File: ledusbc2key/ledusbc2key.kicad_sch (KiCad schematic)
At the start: 25 parts, among them SW1 SW_Push, U1 ATmega32U2-A, U2 PRTR5V0U2X, Y1 Crystal_GND24_Small

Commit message: did a bit today
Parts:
- removed MX3: MX-NoLED, symbol MX_Alps_Hybrid:MX-NoLED
- C7, C8: footprint Capacitor_SMD:C_0805_2012Metric_Pad1.15x1.40mm_HandSolder -> Capacitor_SMD:C_0805_2012Metric_Pad1.18x1.45mm_HandSolder
- MX1, MX2: footprint (none) -> MX_Alps_Hybrid:MX-1U-NoLED
- R4, R5: footprint Resistor_SMD:R_0805_2012Metric_Pad1.15x1.40mm_HandSolder -> Resistor_SMD:R_0805_2012Metric_Pad1.20x1.40mm_HandSolder
- R6: footprint (none) -> Resistor_SMD:R_0805_2012Metric_Pad1.20x1.40mm_HandSolder
- SW1: footprint (none) -> random-keyboard-parts:SKQGADE010
- Y1: footprint (none) -> Crystal:Crystal_SMD_3225-4Pin_3.2x2.5mm_HandSoldering
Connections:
- net COL2: no longer names the net of U1.18 (PB4)

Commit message: finished 2k
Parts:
- MX1, MX2: footprint MX_Alps_Hybrid:MX-1U-NoLED -> MX_Only:MXOnly-1U-Hotswap
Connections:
- net COL0: now also U1.26 (PC4); no longer U1.16 (PB2)
- net COL1: now also U1.25 (PC5); no longer U1.17 (PB3)
- net LED: now also U1.17 (PB3); no longer U1.23 (PC6)
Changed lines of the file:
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@@
     )
   )
-  (global_label "LED" (shape input) (at 97.79 69.85 0) (fields_autoplaced)
+  (global_label "LED" (shape input) (at 97.79 46.99 0) (fields_autoplaced)
     (effects (font (size 1.27 1.27)) (justify left))
-    (property "Intersheet References" "${INTERSHEET_REFS}" (id 0) (at 103.6502 69.7706 0)
+    (property "Intersheet References" "${INTERSHEET_REFS}" (id 0) (at 103.6502 46.9106 0)
       (effects (font (size 1.27 1.27)) (justify left) hide)
     )
@@
     )
   )
-  (global_label "COL0" (shape input) (at 97.79 44.45 0) (fields_autoplaced)
+  (global_label "COL0" (shape input) (at 97.79 64.77 0) (fields_autoplaced)
     (effects (font (size 1.27 1.27)) (justify left))
-    (property "Intersheet References" "${INTERSHEET_REFS}" (id 0) (at 105.0412 44.3706 0)
+    (property "Intersheet References" "${INTERSHEET_REFS}" (id 0) (at 105.0412 64.6906 0)
       (effects (font (size 1.27 1.27)) (justify left) hide)
     )
@@
     )
   )
-  (global_label "COL1" (shape input) (at 97.79 46.99 0) (fields_autoplaced)
+  (global_label "COL1" (shape input) (at 97.79 67.31 0) (fields_autoplaced)
     (effects (font (size 1.27 1.27)) (justify left))
-    (property "Intersheet References" "${INTERSHEET_REFS}" (id 0) (at 105.0412 46.9106 0)
+    (property "Intersheet References" "${INTERSHEET_REFS}" (id 0) (at 105.0412 67.2306 0)
       (effects (font (size 1.27 1.27)) (justify left) hide)
     )
@@
       (effects (font (size 0.508 0.508)))
     )
-    (property "Footprint" "MX_Alps_Hybrid:MX-1U-NoLED" (id 2) (at 114.935 40.005 0)
+    (property "Footprint" "MX_Only:MXOnly-1U-Hotswap" (id 2) (at 114.935 40.005 0)
       (effects (font (size 1.524 1.524)) hide)
     )
@@
       (effects (font (size 0.508 0.508)))
     )
-    (property "Footprint" "MX_Alps_Hybrid:MX-1U-NoLED" (id 2) (at 98.425 40.005 0)
+    (property "Footprint" "MX_Only:MXOnly-1U-Hotswap" (id 2) (at 98.425 40.005 0)
       (effects (font (size 1.524 1.524)) hide)
     )
@@
     )
     (path "/f9445bf9-6026-4cdf-b33a-84c971e8abe4"
-      (reference "MX1") (unit 1) (value "MX-NoLED") (footprint "MX_Alps_Hybrid:MX-1U-NoLED")
+      (reference "MX1") (unit 1) (value "MX-NoLED") (footprint "MX_Only:MXOnly-1U-Hotswap")
     )
     (path "/9652c5be-ceda-40bb-9f68-e3e71dd4d91a"
-      (reference "MX2") (unit 1) (value "MX-NoLED") (footprint "MX_Alps_Hybrid:MX-1U-NoLED")
+      (reference "MX2") (unit 1) (value "MX-NoLED") (footprint "MX_Only:MXOnly-1U-Hotswap")
     )
     (path "/7ad95de5-26a3-4aff-83fa-e71036fd37d6"

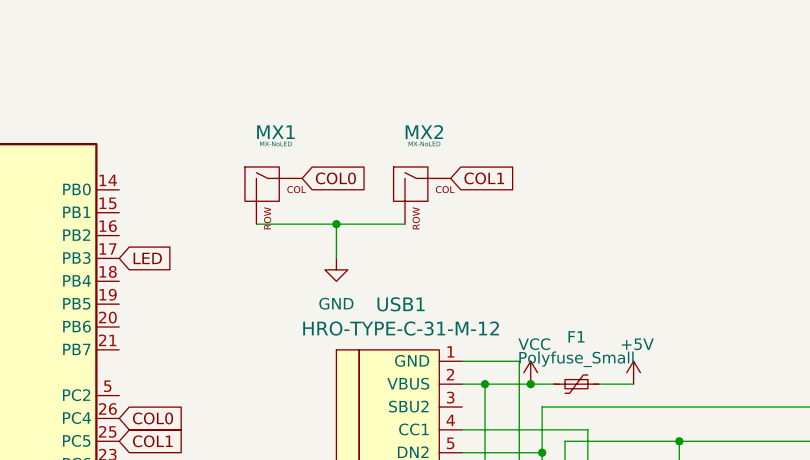
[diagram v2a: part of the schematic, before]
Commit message: swapped to new library for ledusbc
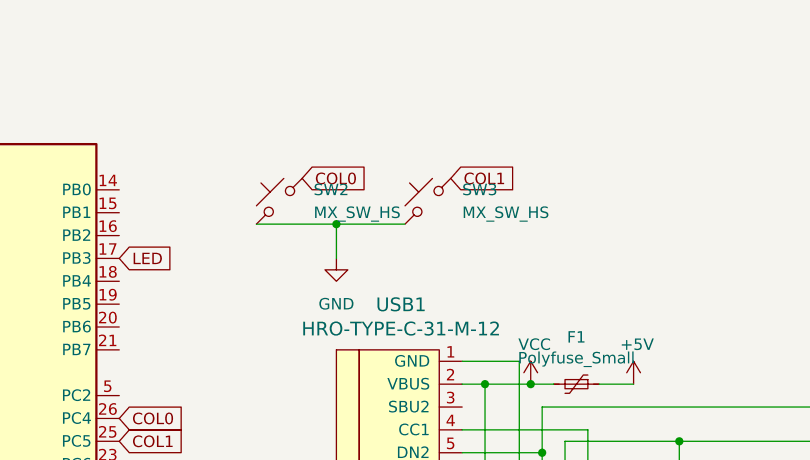
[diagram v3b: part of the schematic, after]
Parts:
- removed MX1, MX2: MX-NoLED, MX_Only:MXOnly-1U-Hotswap, symbol MX_Alps_Hybrid:MX-NoLED
- added SW2, SW3: MX_SW_HS, marbastlib-mx:SW_MX_HS_1u, symbol marbastlib-mx:MX_SW_HS
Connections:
- net COL0: now also SW2.2
- net COL1: now also SW3.2
- net GND: now also SW2.1, SW3.1
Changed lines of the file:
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@@
+    (pin "2")
+  )
+  (symbol (lib_id "marbastlib-mx:MX_SW_HS") (at 115.57 40.64 90) (unit 1)
+    (in_bom yes) (on_board yes) (fields_autoplaced)
+    (property "Reference" "SW2" (id 0) (at 119.38 39.3699 90)
+      (effects (font (size 1.27 1.27)) (justify right))
+    )
+    (property "Value" "MX_SW_HS" (id 1) (at 119.38 41.9099 90)
+      (effects (font (size 1.27 1.27)) (justify right))
+    )
+    (property "Footprint" "marbastlib-mx:SW_MX_HS_1u" (id 2) (at 115.57 40.64 0)
+      (effects (font (size 1.27 1.27)) hide)
+    )
+    (property "Datasheet" "~" (id 3) (at 115.57 40.64 0)
+      (effects (font (size 1.27 1.27)) hide)
+    )
+    (pin "1")
     (pin "2")
   )
@@
     )
     (pin "1")
+  )
+  (symbol (lib_id "marbastlib-mx:MX_SW_HS") (at 132.08 40.64 90) (unit 1)
+    (in_bom yes) (on_board yes) (fields_autoplaced)
+    (property "Reference" "SW3" (id 0) (at 135.89 39.3699 90)
+      (effects (font (size 1.27 1.27)) (justify right))
+    )
+    (property "Value" "MX_SW_HS" (id 1) (at 135.89 41.9099 90)
+      (effects (font (size 1.27 1.27)) (justify right))
+    )
+    (property "Footprint" "marbastlib-mx:SW_MX_HS_1u" (id 2) (at 132.08 40.64 0)
+      (effects (font (size 1.27 1.27)) hide)
+    )
+    (property "Datasheet" "~" (id 3) (at 132.08 40.64 0)
+      (effects (font (size 1.27 1.27)) hide)
+    )
+    (pin "1")
+    (pin "2")
   )
   (symbol (lib_id "power:GND") (at 55.88 73.66 0) (unit 1)
@@
     )
     (pin "1")
-  )
-  (symbol (lib_id "MX_Alps_Hybrid:MX-NoLED") (at 130.81 39.37 0) (unit 1)
-    (in_bom yes) (on_board yes) (fields_autoplaced)
-    (property "Reference" "MX2" (id 0) (at 131.6956 33.02 0)
-      (effects (font (size 1.524 1.524)))
-    )
-    (property "Value" "MX-NoLED" (id 1) (at 131.6956 34.29 0)
-      (effects (font (size 0.508 0.508)))
-    )
-    (property "Footprint" "MX_Only:MXOnly-1U-Hotswap" (id 2) (at 114.935 40.005 0)
-      (effects (font (size 1.524 1.524)) hide)
-    )
-    (property "Datasheet" "" (id 3) (at 114.935 40.005 0)
-      (effects (font (size 1.524 1.524)) hide)
-    )
-    (pin "1")
-    (pin "2")
   )
   (symbol (lib_id "LED:WS2812B") (at 163.83 115.57 0) (unit 1)
@@
     (pin "2")
   )
-  (symbol (lib_id "MX_Alps_Hybrid:MX-NoLED") (at 114.3 39.37 0) (unit 1)
-    (in_bom yes) (on_board yes) (fields_autoplaced)
-    (property "Reference" "MX1" (id 0) (at 115.1856 33.02 0)
-      (effects (font (size 1.524 1.524)))
-    )
-    (property "Value" "MX-NoLED" (id 1) (at 115.1856 34.29 0)
-      (effects (font (size 0.508 0.508)))
-    )
-    (property "Footprint" "MX_Only:MXOnly-1U-Hotswap" (id 2) (at 98.425 40.005 0)
-      (effects (font (size 1.524 1.524)) hide)
-    )
-    (property "Datasheet" "" (id 3) (at 98.425 40.005 0)
-      (effects (font (size 1.524 1.524)) hide)
-    )
-    (pin "1")
-    (pin "2")
-  )
   (sheet_instances
     (path "/" (page "1"))
@@
       (reference "F1") (unit 1) (value "Polyfuse_Small") (footprint "Fuse:Fuse_1206_3216Metric_Pad1.42x1.75mm_HandSolder")
     )
-    (path "/f9445bf9-6026-4cdf-b33a-84c971e8abe4"
-      (reference "MX1") (unit 1) (value "MX-NoLED") (footprint "MX_Only:MXOnly-1U-Hotswap")
-    )
-    (path "/9652c5be-ceda-40bb-9f68-e3e71dd4d91a"
-      (reference "MX2") (unit 1) (value "MX-NoLED") (footprint "MX_Only:MXOnly-1U-Hotswap")
-    )
     (path "/7ad95de5-26a3-4aff-83fa-e71036fd37d6"
       (reference "R1") (unit 1) (value "10k") (footprint "Resistor_SMD:R_0805_2012Metric_Pad1.20x1.40mm_HandSolder")
@@
       (reference "SW1") (unit 1) (value "SW_Push") (footprint "random-keyboard-parts:SKQGADE010")
     )
+    (path "/28cebb3e-b580-4225-a405-e74c4bc8d721"
+      (reference "SW2") (unit 1) (value "MX_SW_HS") (footprint "marbastlib-mx:SW_MX_HS_1u")
+    )
+    (path "/6a80eca7-052b-4f12-ba13-f2e3c6d994ad"
+      (reference "SW3") (unit 1) (value "MX_SW_HS") (footprint "marbastlib-mx:SW_MX_HS_1u")
+    )
     (path "/d060d9ae-df23-483f-83d1-4d8a3c353ba9"
